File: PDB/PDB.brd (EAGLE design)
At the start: 160 x 101.6 mm, 57 parts, among them Q1 NMOS, Q2 IRFML8244, Q3 PMOS, Q4 PMOS, Q5 PMOS

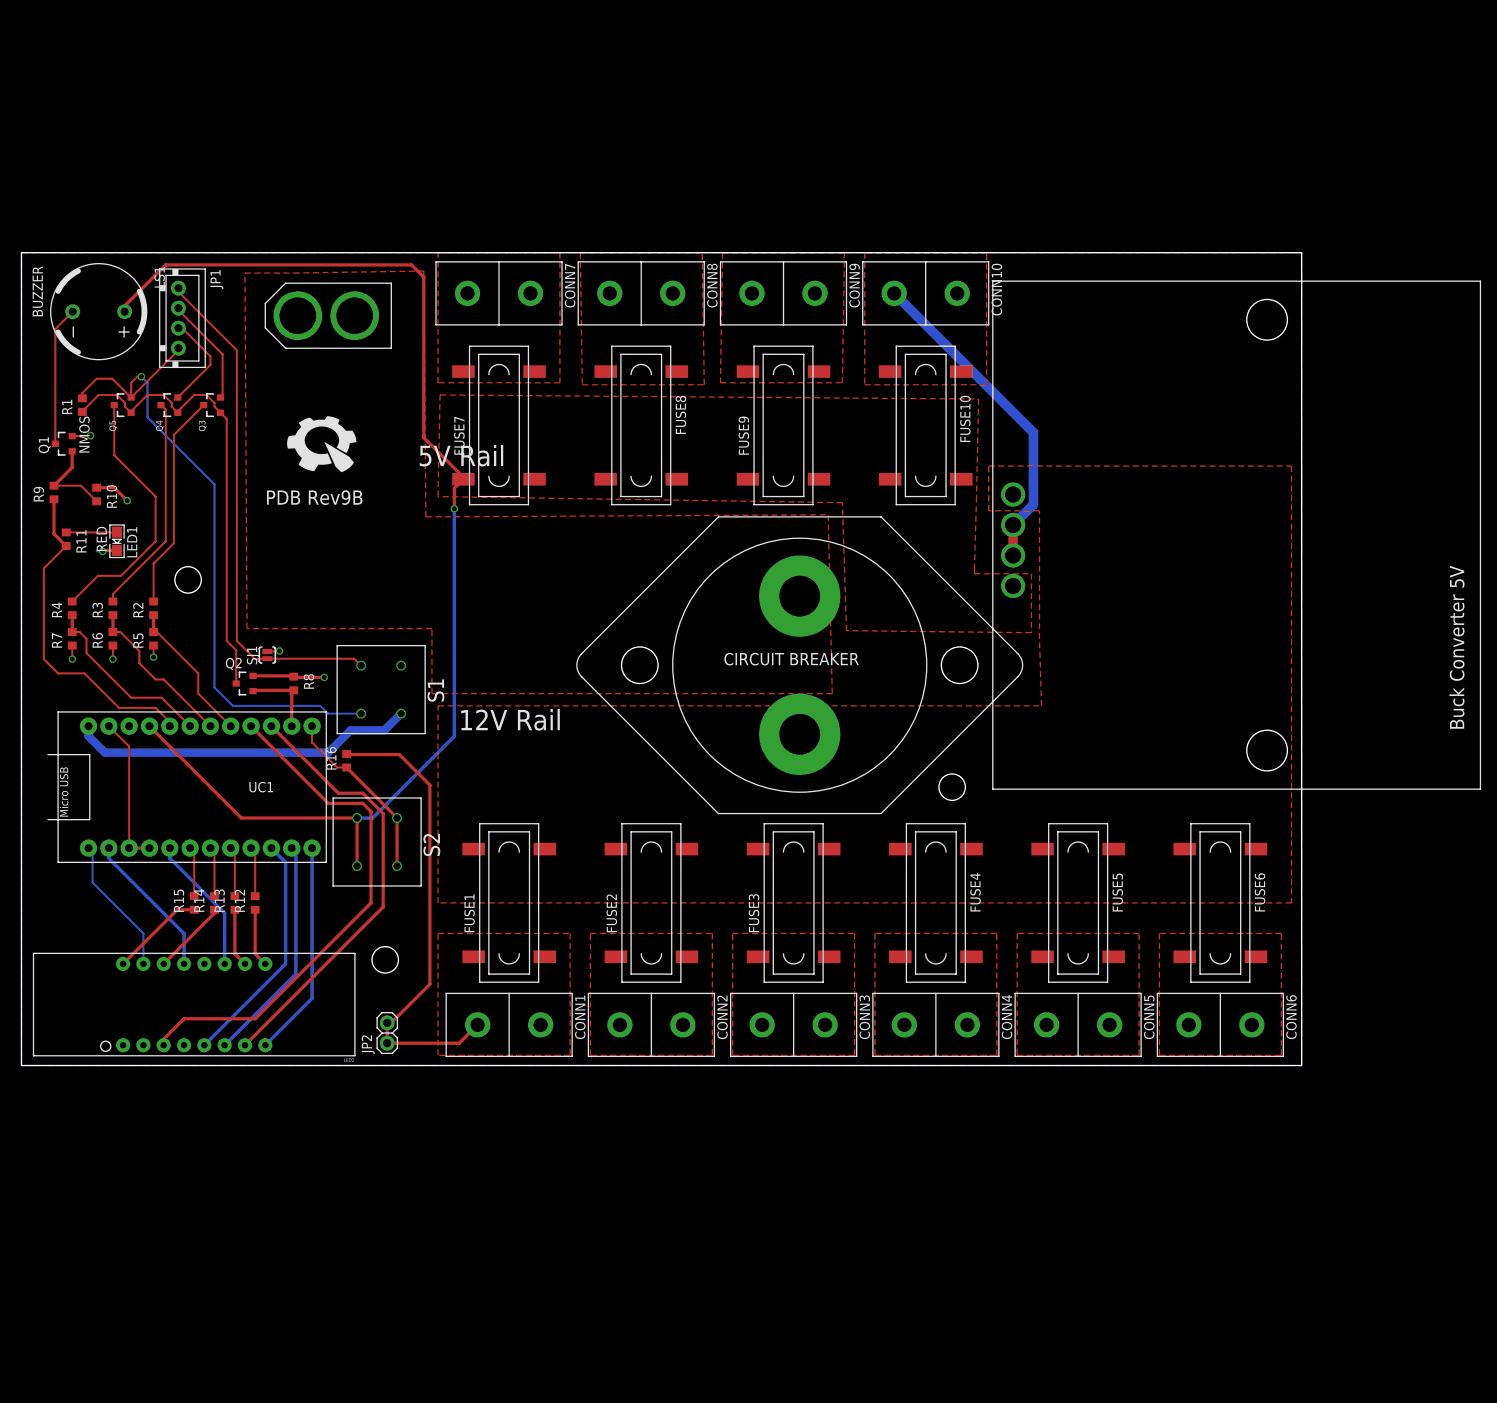
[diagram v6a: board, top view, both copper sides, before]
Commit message: Change Buck Converter mounting hole size and tKeepout, ATX connectors, remove SJ1, add Fuses
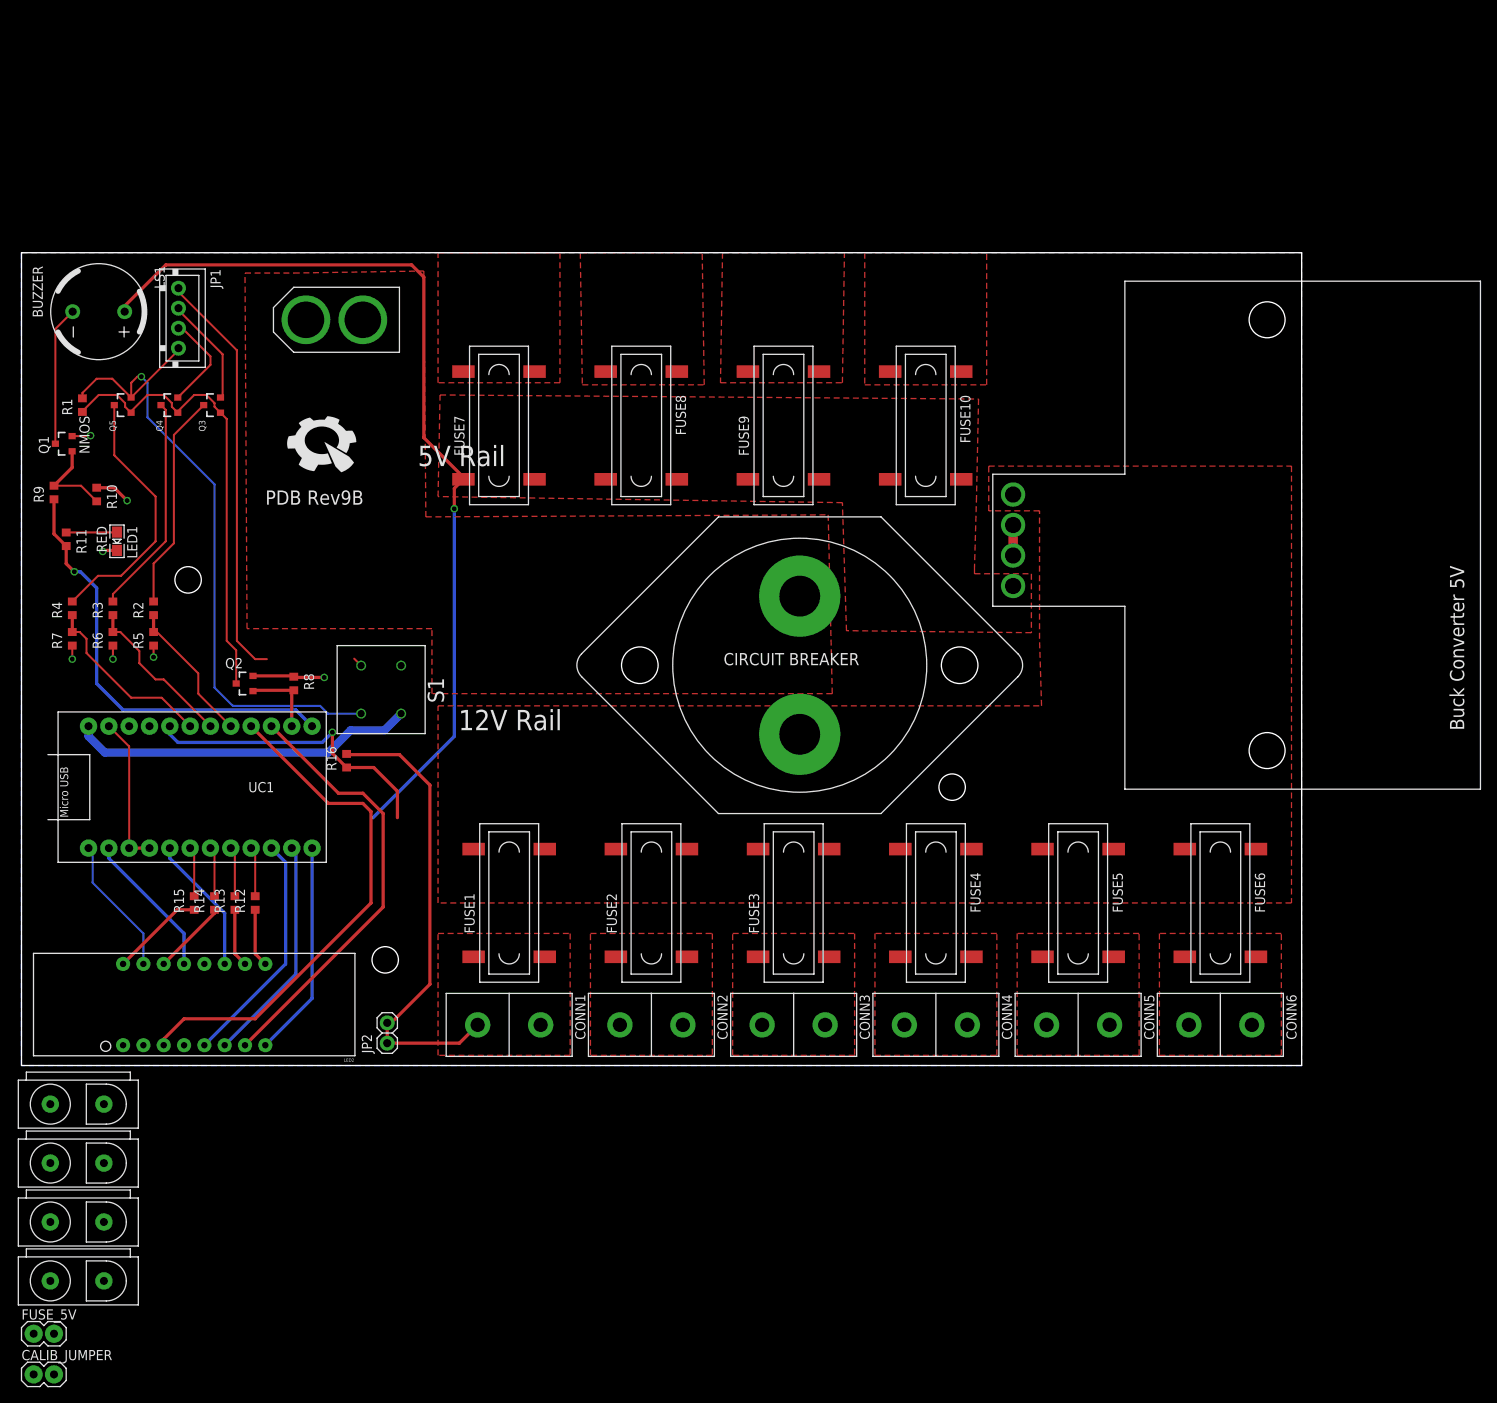
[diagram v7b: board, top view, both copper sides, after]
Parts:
- removed CONN10, CONN7, CONN8, CONN9: ANDERSONVERTICAL, pie:ANDERSON_VERTICAL
- removed S2: DPST_SWITCH, pie:C&K_SWITCH
- removed SJ1: GND to BGND, pie:SJ_2S-NO
- added CALIB_JUMPER, FUSE_5V: JUMPER, pie:JUMPER
- added JP3, JP4, JP5, JP6: ATX, pie:ATX
- moved XT60 1.14 mm to (39.1, 93.2)
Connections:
- new net APM_5V: FUSE_5V.P$1, FUSE_5V.P$2, UC1.VCC
- net 5V: now also CALIB_JUMPER.P$1; no longer S2.P1, S2.P2, UC1.VCC
- net BGND: no longer SJ1.1
- net BUZZER_SIGNAL: now also UC1.10; no longer UC1.A3
- net CALIB: now also CALIB_JUMPER.P$2, UC1.A3; no longer S2.P1', S2.P2', UC1.10
- net GND: now also JP3.P$2, JP4.P$2, JP5.P$2, JP6.P$2; no longer CONN10.PIN1, CONN7.PIN1, CONN8.PIN1, CONN9.PIN1, SJ1.2
- net VOUT10: now also JP6.P$1; no longer CONN10.PIN2
- net VOUT7: now also JP4.P$1; no longer CONN7.PIN2
- net VOUT8: now also JP3.P$1; no longer CONN8.PIN2
- net VOUT9: now also JP5.P$1; no longer CONN9.PIN2
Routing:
- net GND: track 144.1 -> 104.6 mm, vias 8 -> 7
- net 5V: track 155.3 -> 116.7 mm
- net CALIB: track 22.6 -> 38.3 mm, vias 0 -> 1
- net BUZZER_SIGNAL: track 41.3 -> 54.8 mm, vias 0 -> 1
- net BGND: track 64.0 -> 53.0 mm

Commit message: Add resistors 5V Rail; Correct silkscreen
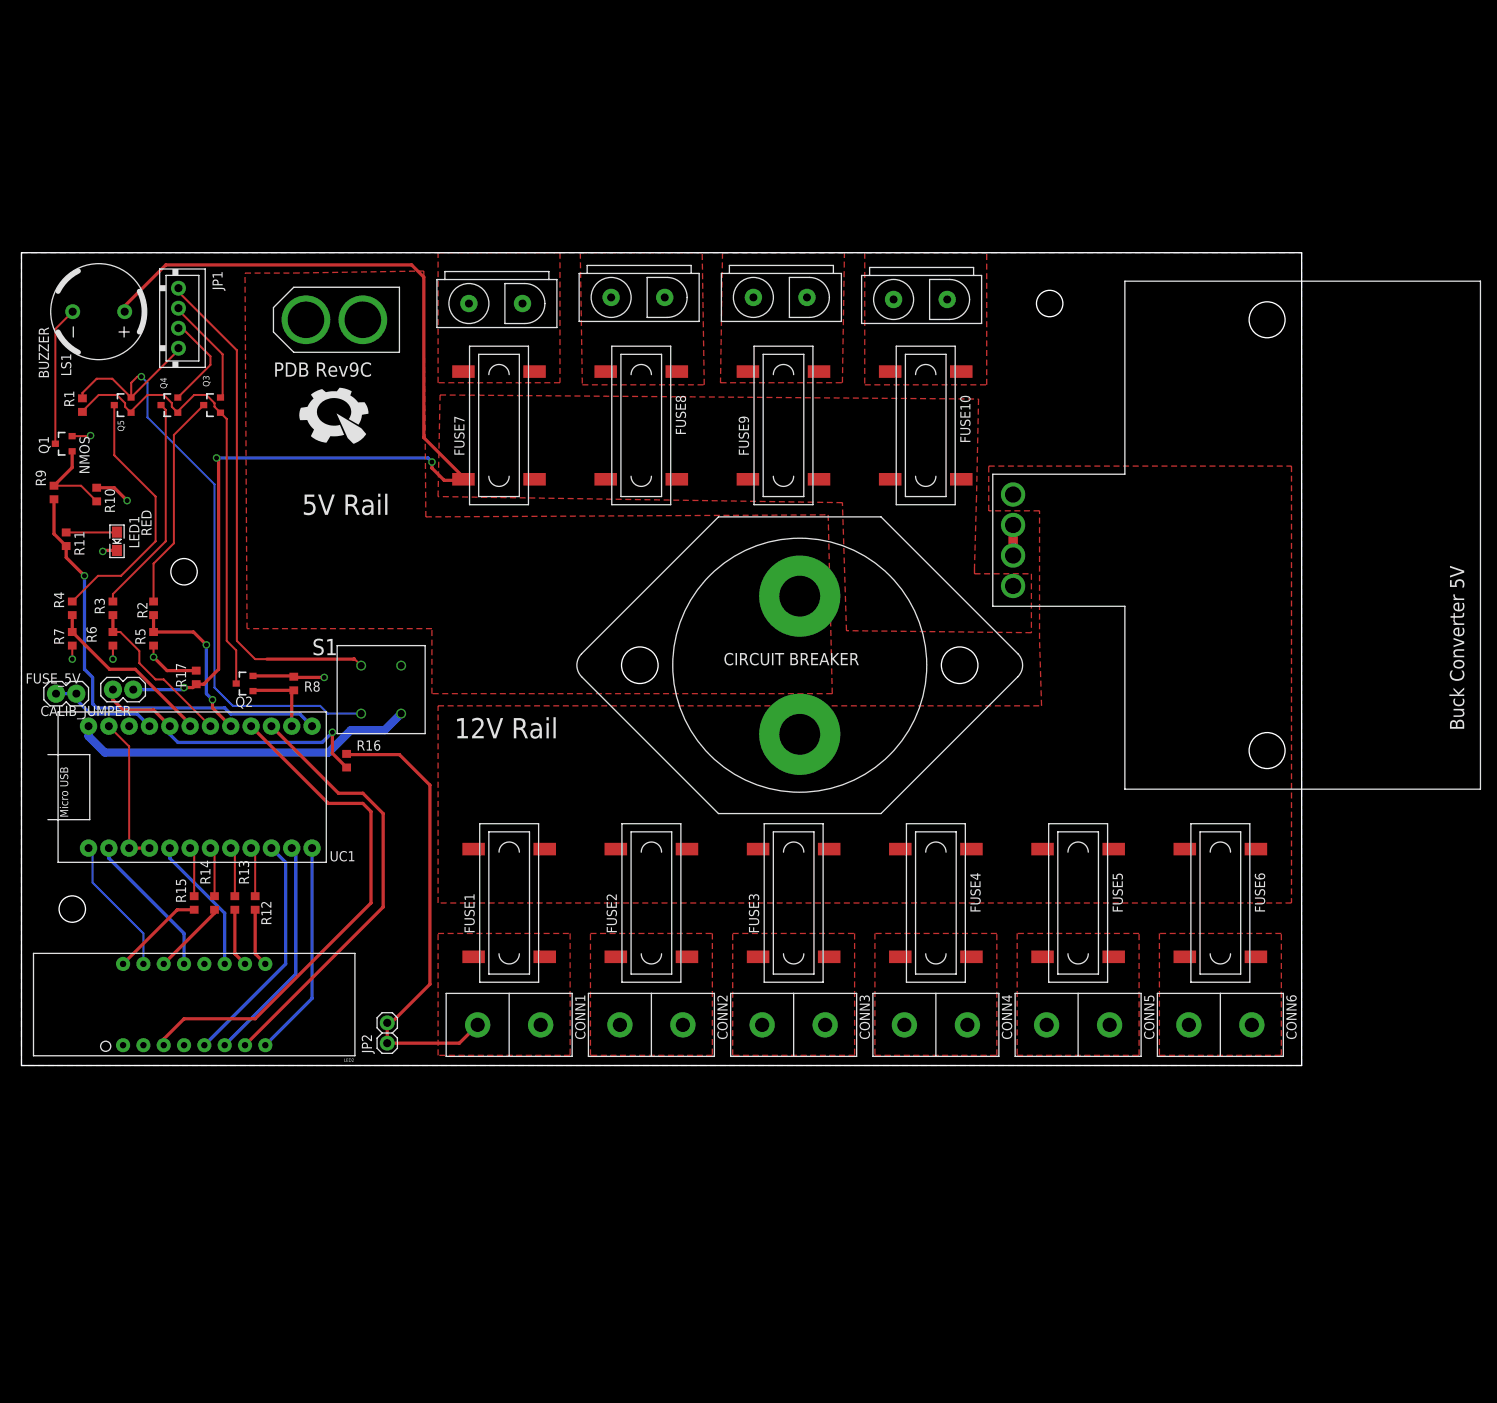
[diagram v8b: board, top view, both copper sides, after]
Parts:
- added R17: (no value), pie:R0603
- moved JP6 161.7 mm to (112.0, 95.8)
- moved JP5 145.2 mm to (94.5, 96.0)
- moved JP3 122.8 mm to (76.7, 96.0)
- moved JP4 119.5 mm to (58.9, 95.2)
- moved CALIB_JUMPER 86.2 mm to (12.7, 47.0), turned to 180 degrees
- moved FUSE_5V 80.1 mm to (5.59, 46.5)
- moved U$4 61.7 mm to (128.5, 95.2)
- moved U$2 39.6 mm to (6.35, 19.6)
- moved U$6 3.87 mm to (39.4, 81.5)
- moved U$5 1.14 mm to (20.3, 61.7)
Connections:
- net 5V: now also R17.1
- net GND: now also R17.2
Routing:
- net 5V: track 116.7 -> 140.4 mm, vias 1 -> 3
- net APM_5V: track 0.00 -> 13.8 mm
- net BGND: track 53.0 -> 64.0 mm
- net GND: track 104.6 -> 110.6 mm
- net IO0: track 18.1 -> 20.8 mm, vias 0 -> 2
- net BUZZER_SIGNAL: track 54.8 -> 56.2 mm
- net CALIB: track 38.3 -> 37.2 mm
- net IO2: track 22.8 -> 21.9 mm
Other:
- board text added: "PDB Rev9C"
- board text removed: "PDB Rev9B"
